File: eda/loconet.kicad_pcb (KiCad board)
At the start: 4 copper layers, 105.7 x 59.2 mm, 78 parts, among them J1 RJ12, J10 DCC IN, J11 DCC1, J12 FROG3, J13 DCC4, J14 FROG4, J15 LN Debug, J16 LN Raw, J2 RJ12, J3 FROG1, J4 DCC2, J5 FROG2, J6 DCC3, J7 RS_SUPL, J8 RS_PUP, J9 12V IN, Q1 MMBT3904, Q2 BC846B, Q3 BC846B, U1 LM311, U2 MOUDLE-SEEEDUINO-XIAO, U3 AMS1117, U4 6N139, U5 6N139, U6 6N139, U7 6N139

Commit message: Fixups
* I removed the additional forwarding power part of the LN schematic. I don't think I was doing it right anyway. use a UP5 instead.
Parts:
- removed D17: SS14, PCM_JLCPCB:D_SMA
- removed D20: 1N4001, Diode_THT:D_DO-41_SOD81_P10.16mm_Horizontal
- removed J7: RS_SUPL, Connector_PinHeader_2.54mm:PinHeader_1x02_P2.54mm_Vertical
- removed J8: RS_PUP, Connector_PinHeader_2.54mm:PinHeader_1x02_P2.54mm_Vertical
- removed Q2, Q3: BC846B, PCM_JLCPCB:Q_SOT-23
- removed R17: 10kΩ, PCM_JLCPCB:R_0603
- removed R18: 47Ω, PCM_JLCPCB:R_0603
- moved D8 31.2 mm to (194.5, 90.5)
- moved TP1 4.27 mm to (194.5, 96.0)
- moved TP3 1.00 mm to (189.5, 88.5)
- turned D6 to 0 degrees
- turned R7 to 0 degrees
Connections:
- net LNET renamed /LNET
- C6 pad 1: +12V -> Net-(U3-VIN)
- D6 pad 2: +12V -> Net-(U3-VIN)
- D8 pad 1: LN1 -> Net-(U3-VIN)
- D8 pad 2: Net-(J7-Pin_1) -> Net-(J9-Pin_1)
- J9 pad 1: Net-(D20-A) -> Net-(J9-Pin_1)
- TP1 pad 1: +12V -> Net-(U3-VIN)
- U3 pad 3: +12V -> Net-(U3-VIN)
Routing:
- net LN2: track 50.3 -> 16.8 mm
- net +12V: track 31.6 -> 0.00 mm, vias 1 -> 0
- net Net-(U3-VIN): track 0.00 -> 28.7 mm
- net Net-(J8-Pin_1): track 12.4 -> 0.00 mm
- net Net-(J9-Pin_1): track 0.00 -> 10.0 mm
- net /LNET: track 53.8 -> 44.1 mm
- net Net-(D20-A): track 8.04 -> 0.00 mm
- net Net-(J7-Pin_1): track 7.08 -> 0.00 mm
- net Net-(Q2-C): track 6.74 -> 0.00 mm
- net Net-(Q2-B): track 3.97 -> 0.00 mm
- net LN1: track 19.3 -> 17.2 mm
- added copper zone on In2.Cu, net Net-(U3-VIN)
- removed copper zone on In2.Cu, net +12V
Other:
- board text added: "9-15V into barrel jack USBC will only provide debug power ***Do not use both at the same time"
- board text added: "GPIO D1 Pin 2"
- board text added: "LN Raw"
- board text added: "LN TP"
- board text added: "VIN"
- board text removed: "+12V"
- board text removed: "12V into barrel jack USBC will only provide debug power ***Do not use both at the same time"
- board text removed: "GPIO D1 Pin 1"

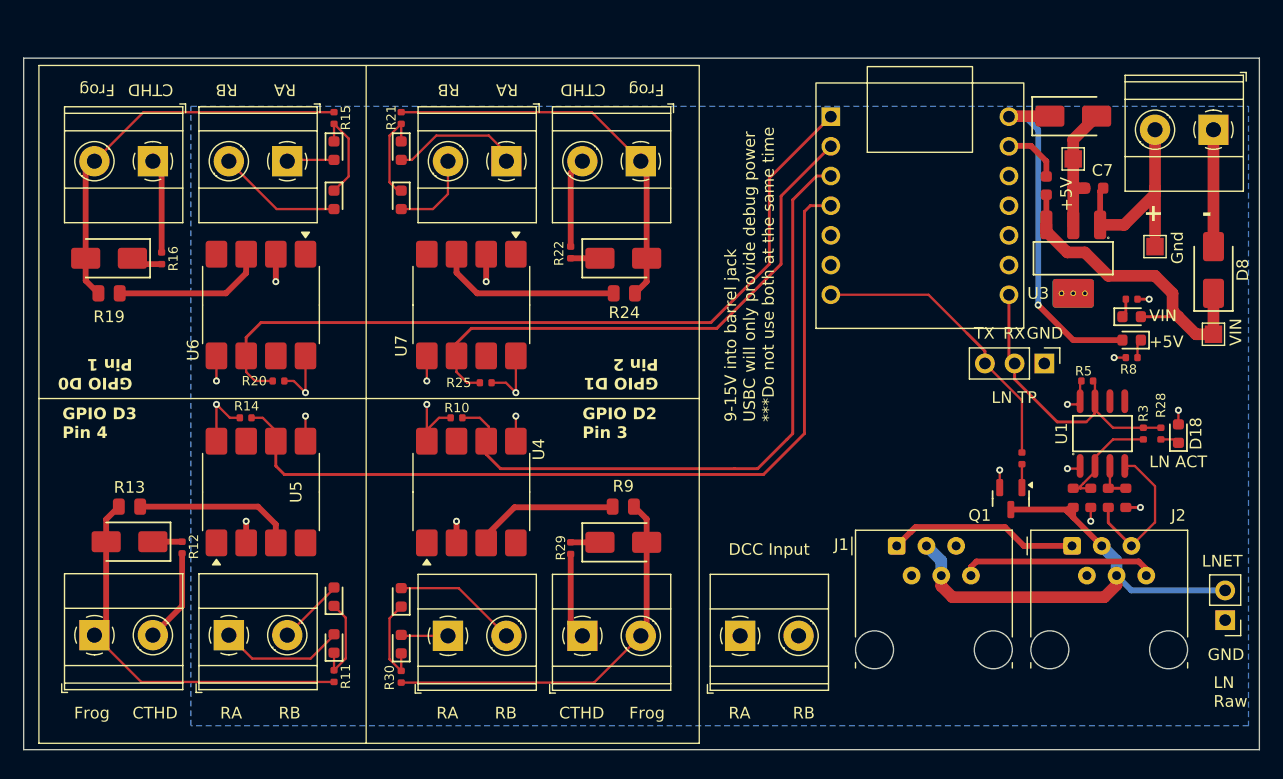
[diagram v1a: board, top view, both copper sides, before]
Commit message: Updating to the latest version of the board, still in KiCad 8.
* Bumped the README to be more readable.
* Removed second RJ12 jack, no more forwarding.
* Small changes to the ino.wq
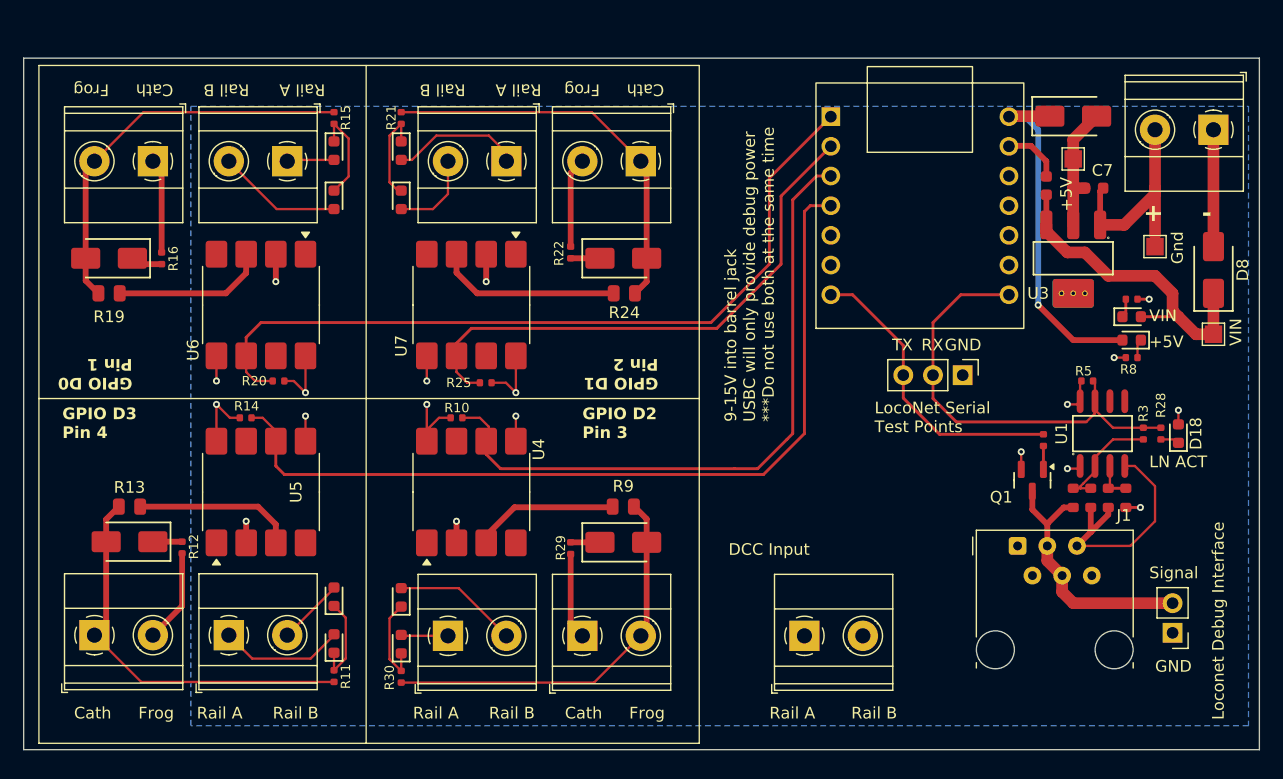
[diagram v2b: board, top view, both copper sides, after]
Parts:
- removed the J1 at (167.4, 114.1)
- moved J15 7.06 mm to (173.0, 99.5)
- moved J10 5.50 mm to (159.5, 121.8)
- moved J1 4.66 mm to (177.7, 114.1)
- moved J16 4.63 mm to (191.0, 121.5)
- moved Q1 2.41 mm to (179.0, 108.5)
- moved R23 2.41 mm to (179.9, 105.1)
- renumbered J2 to J1
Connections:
- J1 pad 1: LN1 -> unconnected-(J1-Pad1)
- J1 pad 6: LN2 -> unconnected-(J1-Pad6)
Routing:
- net /LNET: track 44.1 -> 22.4 mm
- net LN1: track 17.2 -> 0.00 mm
- net LN2: track 16.8 -> 0.00 mm
- net RX: track 26.0 -> 38.8 mm
- net GND: track 52.0 -> 58.2 mm, vias 9 -> 8
- net TX: track 25.2 -> 25.8 mm
- removed copper zone on In2.Cu, net Net-(U3-VIN)
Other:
- board text added: "Cath"
- board text added: "LocoNet Serial Test Points"
- board text added: "Loconet Debug Interface"
- board text added: "Rail A"
- board text added: "Rail B"
- board text added: "Signal"
- board text removed: "CTHD"
- board text removed: "LN Raw"
- board text removed: "LN TP"
- board text removed: "LNET"
- board text removed: "RA"
- board text removed: "RB"

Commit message: Fixing issues with the layout after moving to KiCad 9
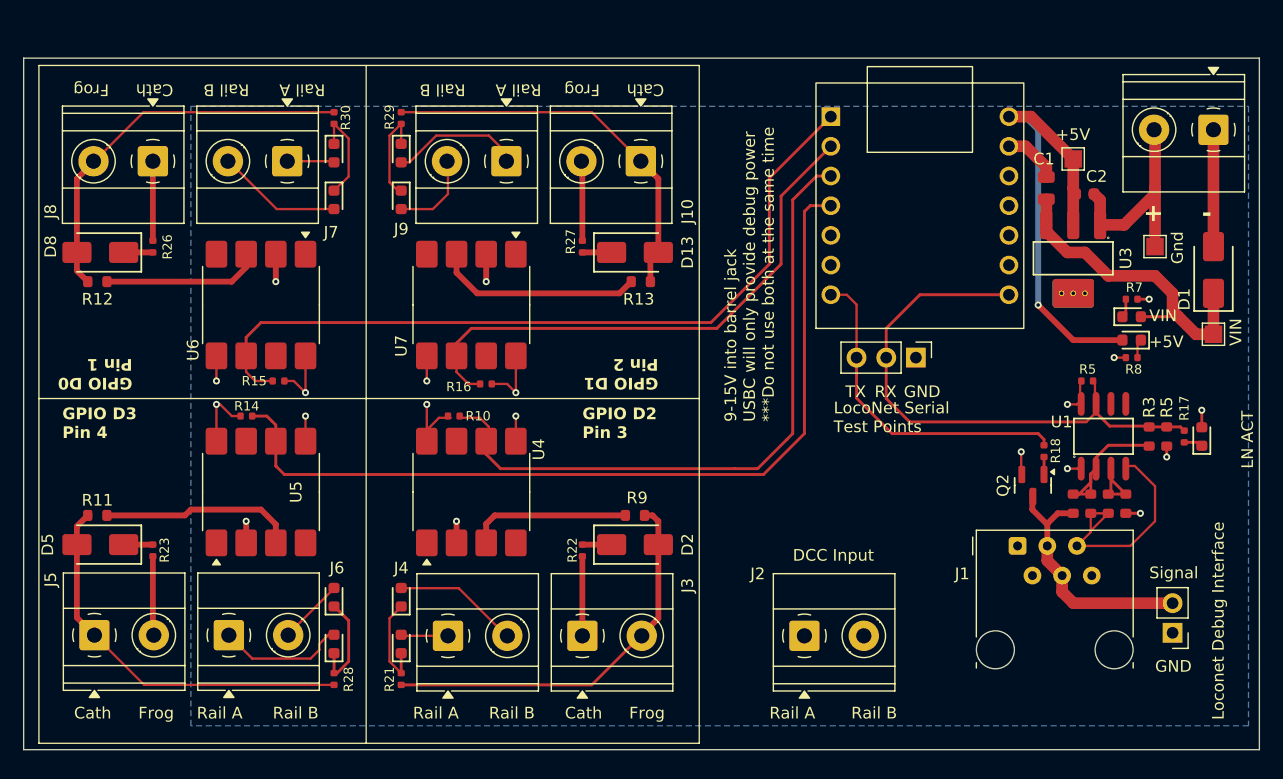
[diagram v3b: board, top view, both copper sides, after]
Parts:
- removed C6, C7: 22uF, PCM_JLCPCB:C_0603
- removed D15: Green, PCM_JLCPCB:D_0603
- removed D18: Yellow, PCM_JLCPCB:D_0603
- removed Q1: MMBT3904, PCM_JLCPCB:Q_SOT-23
- removed R19, R24: 510Ω, PCM_JLCPCB:R_0805
- removed R20, R25: 4.7kΩ, PCM_JLCPCB:R_0402
- added C1: 22uF, PCM_JLCPCB:C_0805, F.Cu at (180.2, 83.5)
- added C2: 22uF, PCM_JLCPCB:C_0603, F.Cu at (183.5, 84.0)
- added D17: Red, PCM_JLCPCB:D_0603, F.Cu at (125.0, 84.5)
- added Q2: MMBT3904, PCM_JLCPCB:Q_SOT-23, F.Cu at (179.1, 108.9)
- added R17: 1kΩ, PCM_JLCPCB:R_0402, F.Cu at (192.0, 104.8)
- added R18: 2kΩ, PCM_JLCPCB:R_0402, F.Cu at (180.0, 106.0)
- added R26: 2kΩ, PCM_JLCPCB:R_0402, F.Cu at (103.8, 88.5)
- added R27: 2kΩ, PCM_JLCPCB:R_0402, F.Cu at (140.5, 88.5)
- added R5: 10kΩ, PCM_JLCPCB:R_0603, F.Cu at (190.5, 104.8)
- D16: value SS14 -> Yellow; footprint PCM_JLCPCB:D_SMA -> PCM_JLCPCB:D_0603
- D3: value Red -> Green
- J10: renamed from J14; footprint TerminalBlock_Phoenix:TerminalBlock_Phoenix_MKDS-1,5-2_1x02_P5.00mm_Horizontal -> TerminalBlock_Phoenix:TerminalBlock_Phoenix_MKDS-1,5-2-5.08_1x02_P5.08mm_Horizontal
- J13: renamed from J9; footprint TerminalBlock_Phoenix:TerminalBlock_Phoenix_MKDS-1,5-2_1x02_P5.00mm_Horizontal -> TerminalBlock_Phoenix:TerminalBlock_Phoenix_MKDS-1,5-2-5.08_1x02_P5.08mm_Horizontal
- J2: renamed from J10; footprint TerminalBlock_Phoenix:TerminalBlock_Phoenix_MKDS-1,5-2_1x02_P5.00mm_Horizontal -> TerminalBlock_Phoenix:TerminalBlock_Phoenix_MKDS-1,5-2-5.08_1x02_P5.08mm_Horizontal
- J3, J5: footprint TerminalBlock_Phoenix:TerminalBlock_Phoenix_MKDS-1,5-2_1x02_P5.00mm_Horizontal -> TerminalBlock_Phoenix:TerminalBlock_Phoenix_MKDS-1,5-2-5.08_1x02_P5.08mm_Horizontal
- J4: renamed from J11; footprint TerminalBlock_Phoenix:TerminalBlock_Phoenix_MKDS-1,5-2_1x02_P5.00mm_Horizontal -> TerminalBlock_Phoenix:TerminalBlock_Phoenix_MKDS-1,5-2-5.08_1x02_P5.08mm_Horizontal
- J6: renamed from J4; footprint TerminalBlock_Phoenix:TerminalBlock_Phoenix_MKDS-1,5-2_1x02_P5.00mm_Horizontal -> TerminalBlock_Phoenix:TerminalBlock_Phoenix_MKDS-1,5-2-5.08_1x02_P5.08mm_Horizontal
- J7: renamed from J6; footprint TerminalBlock_Phoenix:TerminalBlock_Phoenix_MKDS-1,5-2_1x02_P5.00mm_Horizontal -> TerminalBlock_Phoenix:TerminalBlock_Phoenix_MKDS-1,5-2-5.08_1x02_P5.08mm_Horizontal
- J8: renamed from J12; footprint TerminalBlock_Phoenix:TerminalBlock_Phoenix_MKDS-1,5-2_1x02_P5.00mm_Horizontal -> TerminalBlock_Phoenix:TerminalBlock_Phoenix_MKDS-1,5-2-5.08_1x02_P5.08mm_Horizontal
- J9: renamed from J13; footprint TerminalBlock_Phoenix:TerminalBlock_Phoenix_MKDS-1,5-2_1x02_P5.00mm_Horizontal -> TerminalBlock_Phoenix:TerminalBlock_Phoenix_MKDS-1,5-2-5.08_1x02_P5.08mm_Horizontal
- R11, R12: value 2kΩ -> 510Ω; footprint PCM_JLCPCB:R_0402 -> PCM_JLCPCB:R_0603
- R13, R9: footprint PCM_JLCPCB:R_0805 -> PCM_JLCPCB:R_0603
- R15, R16: value 2kΩ -> 4.7kΩ
- R28: value 1kΩ -> 2kΩ
- R3: footprint PCM_JLCPCB:R_0402 -> PCM_JLCPCB:R_0603
- moved D8 95.3 mm to (99.2, 89.0), turned to 180 degrees
- moved R23 76.8 mm to (103.8, 114.5)
- moved R28 73.8 mm to (119.2, 125.5)
- moved D16 51.8 mm to (193.5, 104.8), turned to 90 degrees
- moved R30 48.1 mm to (119.2, 77.5), turned to 90 degrees
- moved R21 48.0 mm to (125.0, 125.5), turned to -90 degrees
- moved R13 47.8 mm to (145.5, 91.5), turned to 180 degrees
- moved D13 45.0 mm to (145.0, 89.0), turned to 0 degrees
- moved D9 42.4 mm to (119.2, 80.5), turned to -90 degrees
- moved R29 39.6 mm to (125.0, 77.5)
- moved D11 34.0 mm to (119.2, 118.5), turned to 90 degrees
- moved R16 29.8 mm to (132.2, 100.2), turned to 180 degrees
- moved R22 25.5 mm to (140.5, 114.5), turned to 90 degrees
- moved R11 24.5 mm to (99.0, 111.5), turned to 0 degrees
- moved R12 23.9 mm to (99.0, 91.5), turned to 0 degrees
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- renumbered J15 to J11, J16 to J12
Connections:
- D1 pad 1: +5V -> Net-(U3-VIN)
- D1 pad 2: Net-(U3-VOUT) -> Net-(J13-Pin_1)
- D12 pad 1: Net-(D11-Pad1) -> Net-(D12-Pad1)
- D13 pad 2: Net-(J12-Pin_2) -> Net-(J10-Pin_1)
- D16 pad 2: Net-(J14-Pin_1) -> +3V3
- D3 pad 1: Net-(D3-Pad1) -> Net-(D10-Pad1)
- D3 pad 2: DCC_B -> DCC_A
- D4 pad 1: Net-(D3-Pad1) -> Net-(D11-Pad1)
- D8 pad 1: Net-(U3-VIN) -> Net-(D8-Pad1)
- D8 pad 2: Net-(J9-Pin_1) -> Net-(J8-Pin_2)
- D9 pad 1: Net-(D10-Pad1) -> Net-(D14-Pad1)
- J10 pad 1: Net-(J14-Pin_1) -> Net-(J10-Pin_1)
- J10 pad 2: Net-(J14-Pin_2) -> Net-(J10-Pin_2)
- J13 pad 1: Net-(J9-Pin_1) -> Net-(J13-Pin_1)
- J8 pad 1: Net-(J12-Pin_1) -> Net-(J8-Pin_1)
- J8 pad 2: Net-(J12-Pin_2) -> Net-(J8-Pin_2)
- R11 pad 1: Net-(D3-Pad1) -> Net-(J5-Pin_1)
- R11 pad 2: Net-(J5-Pin_1) -> Net-(U5-C2)
- R12 pad 1: Net-(J5-Pin_2) -> Net-(J8-Pin_2)
- R12 pad 2: Net-(D5-Pad1) -> Net-(U6-C2)
- R13 pad 1: Net-(J5-Pin_1) -> Net-(J10-Pin_1)
- R13 pad 2: Net-(U5-C2) -> Net-(U7-C2)
- R15 pad 1: Net-(D11-Pad1) -> +3V3
- R15 pad 2: Net-(J12-Pin_2) -> DIP_STATE_3
- R16 pad 1: Net-(J12-Pin_1) -> +3V3
- R16 pad 2: Net-(D13-Pad1) -> DIP_STATE_4
- R21 pad 1: Net-(D14-Pad1) -> Net-(D10-Pad1)
- R21 pad 2: Net-(J14-Pin_1) -> Net-(J3-Pin_2)
- R22 pad 1: Net-(J14-Pin_2) -> Net-(J3-Pin_1)
- R22 pad 2: Net-(D16-Pad1) -> Net-(D2-Pad1)
- R23 pad 1: Net-(Q1-B) -> Net-(J5-Pin_2)
- R23 pad 2: TX -> Net-(D5-Pad1)
- R28 pad 1: RX -> Net-(D11-Pad1)
- R28 pad 2: Net-(D18-Pad1) -> Net-(J5-Pin_1)
- R29 pad 1: Net-(J3-Pin_1) -> Net-(D12-Pad1)
- R29 pad 2: Net-(D2-Pad1) -> Net-(J10-Pin_1)
- R30 pad 1: Net-(D10-Pad1) -> Net-(D14-Pad1)
- R30 pad 2: Net-(J3-Pin_2) -> Net-(J8-Pin_2)
- R8 pad 1: GND -> Net-(D7-Pad1)
- R8 pad 2: Net-(D7-Pad1) -> GND
- TP2 pad 1: Net-(U3-VOUT) -> +5V
- U3 pad 2: Net-(U3-VOUT) -> +5V
- U3 pad 4: (no net) -> unconnected-(U3-VOUT-Pad4)_3
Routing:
- net Net-(J12-Pin_2): track 34.3 -> 0.00 mm
- net Net-(J14-Pin_1): track 34.2 -> 0.00 mm
- net Net-(J8-Pin_2): track 0.00 -> 33.5 mm
- net Net-(J10-Pin_1): track 0.00 -> 33.4 mm
- net Net-(U3-VOUT): track 11.1 -> 0.00 mm
- net RX: track 38.8 -> 49.1 mm
- net Net-(J9-Pin_1): track 10.0 -> 0.00 mm
- net Net-(J13-Pin_1): track 0.00 -> 10.0 mm
- net +5V: track 30.5 -> 39.3 mm
- net Net-(D12-Pad1): track 0.00 -> 8.42 mm
- net Net-(D3-Pad1): track 8.33 -> 0.00 mm
- net Net-(J12-Pin_1): track 8.12 -> 0.00 mm
- net Net-(J14-Pin_2): track 7.72 -> 0.00 mm
- net Net-(J8-Pin_1): track 0.00 -> 6.81 mm
- net Net-(J10-Pin_2): track 0.00 -> 6.81 mm
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
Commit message: Design fixups
* LDO was too limited in input voltage, switch to a part with a bigger input voltage
* Update README
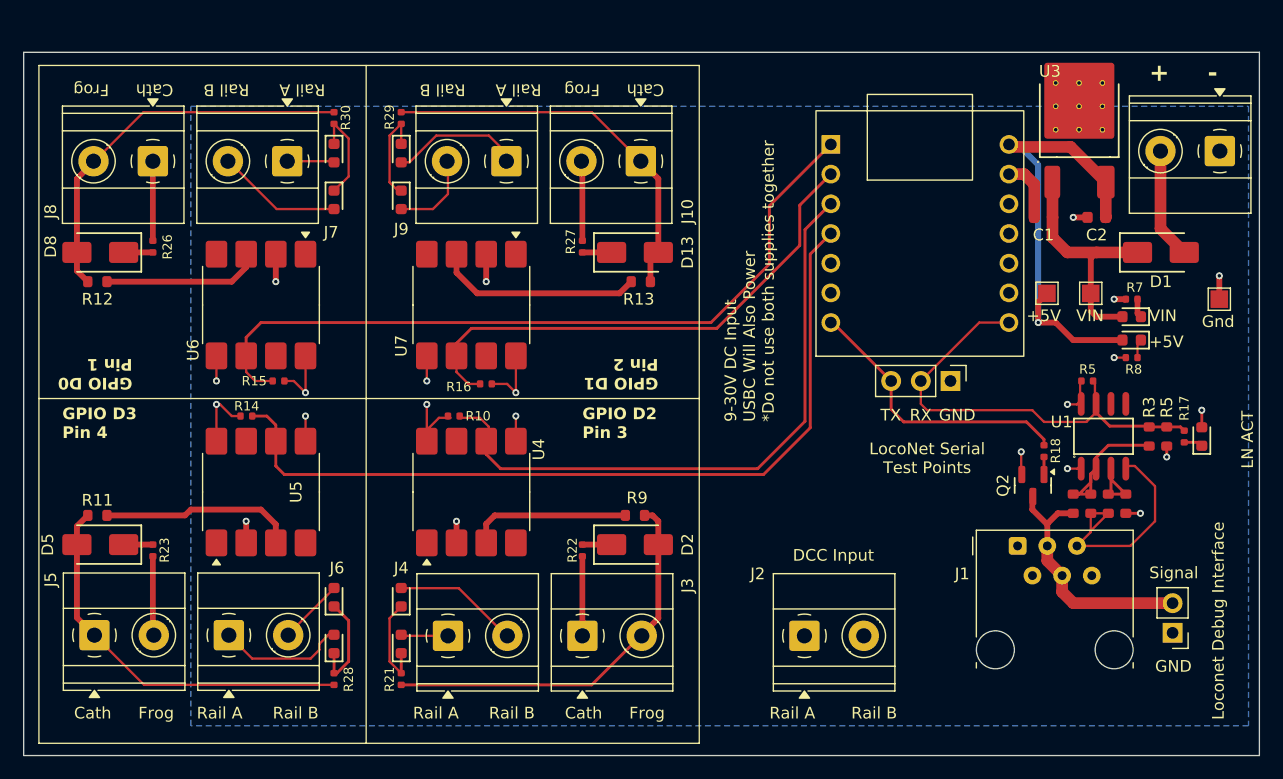
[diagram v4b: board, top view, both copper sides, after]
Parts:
- C1: value 22uF -> 330nF; footprint PCM_JLCPCB:C_0805 -> PCM_JLCPCB:C_0603
- C2: value 22uF -> 100nF
- J13: value 12V IN -> Input voltage
- U3: value AMS1117 -> L78M05ABDT-TR; footprint PCM_JLCPCB:SOT-223_L6.5-W3.5-P2.30-LS7.0-BR -> PCM_JLCPCB:TO-252-2_L6.5-W6.1-P4.58-LS10.0-TL
- moved TP2 11.7 mm to (180.2, 92.5)
- moved TP1 11.1 mm to (184.0, 92.5)
- moved U3 10.0 mm to (183.0, 79.5)
- moved TP3 7.11 mm to (195.0, 93.0)
- moved D1 4.74 mm to (190.0, 89.0), turned to 0 degrees
- moved J11 3.57 mm to (172.0, 100.0)
- moved C1 2.51 mm to (179.9, 86.0), turned to 180 degrees
- moved U2 2.38 mm to (169.4, 87.4)
- moved C2 2.24 mm to (184.5, 86.0), turned to 180 degrees
- moved J13 1.91 mm to (195.0, 80.3)
- turned D6 to 180 degrees
- turned R7 to 180 degrees
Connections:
- D1 pad 2: Net-(J13-Pin_1) -> Net-(J13-Pin_2)
- J13 pad 1: Net-(J13-Pin_1) -> GND
- J13 pad 2: GND -> Net-(J13-Pin_2)
- U3 pad 1: GND -> Net-(U3-VIN)
- U3 pad 3: Net-(U3-VIN) -> +5V
- U3 pad 4: unconnected-(U3-VOUT-Pad4)_3 -> GND
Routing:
- net GND: track 57.8 -> 43.4 mm, vias 8 -> 10
- net Net-(J13-Pin_1): track 10.0 -> 0.00 mm
- net Net-(J13-Pin_2): track 0.00 -> 9.52 mm
- net RX: track 49.1 -> 39.9 mm
- net Net-(U3-VIN): track 28.3 -> 20.7 mm
- net TX: track 28.6 -> 24.3 mm
- net DIP_STATE_2: track 75.2 -> 71.8 mm
- net DIP_STATE_1: track 57.2 -> 54.1 mm
- net DIP_STATE_3: track 67.7 -> 65.3 mm
- net DIP_STATE_4: track 47.3 -> 44.9 mm
- net +5V: track 39.3 -> 40.0 mm
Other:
- board size 105.7 x 59.2 mm -> 105.7 x 60.2 mm
- board text added: "9-30V DC Input USBC Will Also Power *Do not use both supplies together"
- board text removed: "9-15V into barrel jack USBC will only provide debug power ***Do not use both at the same time"
